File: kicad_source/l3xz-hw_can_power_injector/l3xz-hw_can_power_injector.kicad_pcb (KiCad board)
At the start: 2 copper layers, 43 x 23 mm, 17 parts, among them CN1 Conn_01x02, CN2 Conn_01x04, CN3 Conn_01x04, U1 RAA211650

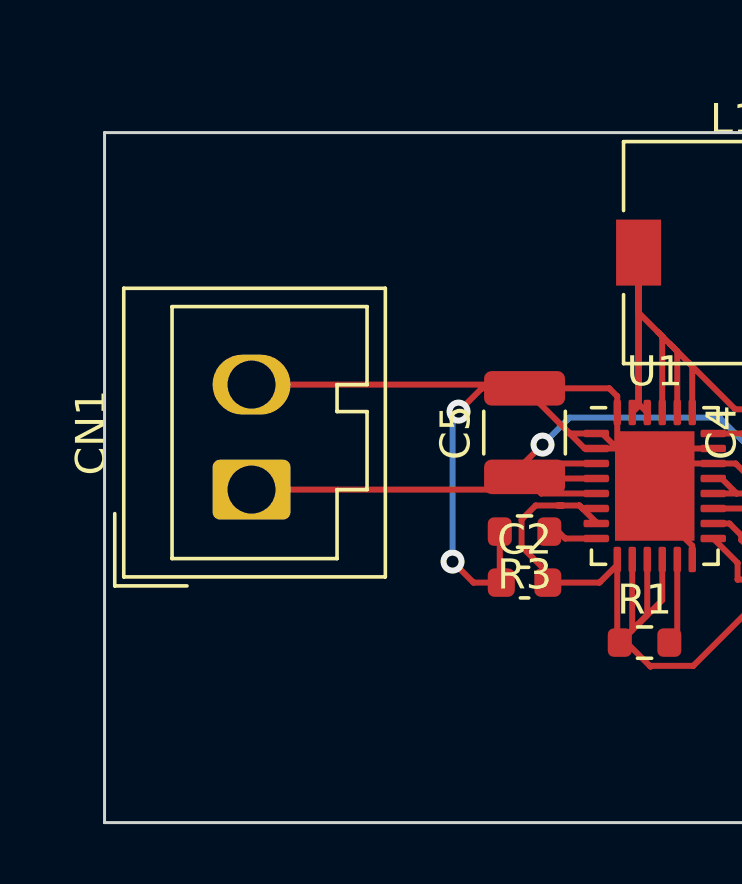
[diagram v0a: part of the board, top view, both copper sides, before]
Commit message: added Powerpole connector
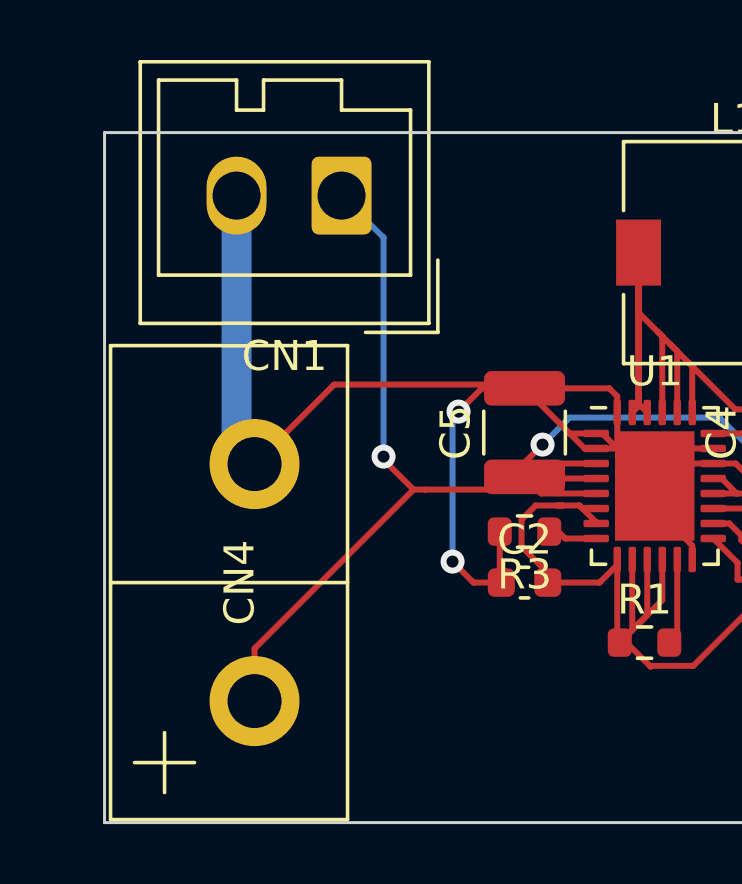
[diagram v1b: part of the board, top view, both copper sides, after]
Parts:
- added CN4: Conn_01x02, generationmake:POWERPOLE_2, F.Cu at (97.0, 102.0)
- moved CN1 10.2 mm to (99.9, 89.1), turned to 180 degrees
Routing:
- net +BATT: track 35.9 -> 50.6 mm, vias 2 -> 3
- net GND: track 101.6 -> 111.8 mm
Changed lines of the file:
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@@
   )
   (paper "A4")
+  (title_block
+    (title "l3xz-hw_can_power_injector")
+    (date "2022-10-25")
+    (rev "0.1")
+    (company "107-systems")
+  )
   (layers
     (0 "F.Cu" signal)
@@
     )
   )
+  (footprint "generationmake:POWERPOLE_2" (layer "F.Cu")
+    (at 97 102 90)
+    (property "Sheetfile" "Datei: l3xz-hw_can_power_injector.kicad_sch")
+    (property "Sheetname" "")
+    (attr through_hole)
+    (fp_text reference "CN4" (at 0 -0.5 90 unlocked) (layer "F.SilkS")
+      (effects (font (size 1 1) (thickness 0.15)))
+    )
+    (fp_text value "Conn_01x02" (at 0 1 90 unlocked) (layer "F.Fab")
+      (effects (font (size 1 1) (thickness 0.15)))
+    )
+    (fp_text user "${REFERENCE}" (at 0 2.5 90 unlocked) (layer "F.Fab")
+      (effects (font (size 1 1) (thickness 0.15)))
+    )
+    (fp_line (start 0 3.1) (end 0 -4.8) (layer "F.SilkS") (width 0.12))
+    (fp_line (start -7.9 3.1) (end 7.9 3.1) (layer "F.SilkS") (width 0.12))
+    (fp_line (start 7.9 3.1) (end 7.9 -4.8) (layer "F.SilkS") (width 0.12))
+    (fp_line (start 7.9 -4.8) (end -7.9 -4.8) (layer "F.SilkS") (width 0.12))
+    (fp_line (start -7.9 -4.8) (end -7.9 3.1) (layer "F.SilkS") (width 0.12))
+    (fp_line (start -7 -3) (end -5 -3) (layer "F.SilkS") (width 0.12))
+    (fp_line (start -6 -4) (end -6 -2) (layer "F.SilkS") (width 0.12))
+    (pad "1" thru_hole circle (at -3.95 0 90) (size 3 3) (drill 1.8) (layers *.Cu *.Mask)
+      (net 1 "+BATT") (pinfunction "Pin_1") (pintype "passive"))
+    (pad "2" thru_hole circle (at 3.95 0 90) (size 3 3) (drill 1.8) (layers *.Cu *.Mask)
+      (net 2 "GND") (pinfunction "Pin_2") (pintype "passive"))
+    (model "${KICAD6_3DMODEL_DIR}/generationmake/PP 15-45 (Std)-02-08-STEP.stp"
+      (offset (xyz 3.95 12.8 12))
+      (scale (xyz 1 1 1))
+      (rotate (xyz 90 0 0))
+    )
+    (model "${KICAD6_3DMODEL_DIR}/generationmake/PP 15-45 (Std)-02-08-STEP.stp"
+      (offset (xyz -3.95 12.8 12))
+      (scale (xyz 1 1 1))
+      (rotate (xyz 90 0 0))
+    )
+  )
   (footprint "Connector_Wago:Wago_734-132_1x02_P3.50mm_Vertical" (layer "F.Cu")
-    (at 96.9 98.9 90)
+    (at 99.9 89.1 180)
     (descr "Molex 734 Male header (for PCBs); Straight solder pin 1 x 1 mm, 734-132 , 2 Pins (http://www.farnell.com/datasheets/2157639.pdf), generated with kicad-footprint-generator")
     (tags "connector Wago  side entry")
@@
     (property "Sheetname" "")
     (attr through_hole)
-    (fp_text reference "CN1" (at 1.9 -5.35 90) (layer "F.SilkS")
-      (effects (font (size 1 1) (thickness 0.15)))
-    )
-    (fp_text value "Conn_01x02" (at 1.9 5.55 90) (layer "F.Fab")
-      (effects (font (size 1 1) (thickness 0.15)))
-    )
-    (fp_text user "${REFERENCE}" (at 1.9 3.65 90) (layer "F.Fab")
+    (fp_text reference "CN1" (at 1.9 -5.35) (layer "F.SilkS")
+      (effects (font (size 1 1) (thickness 0.15)))
+    )
+    (fp_text value "Conn_01x02" (at 1.9 5.55) (layer "F.Fab")
+      (effects (font (size 1 1) (thickness 0.15)))
+    )
+    (fp_text user "${REFERENCE}" (at 1.9 3.65) (layer "F.Fab")
       (effects (font (size 1 1) (thickness 0.15)))
     )
@@
     (fp_line (start -0.5 -4.15) (end 0 -3.442893) (layer "F.Fab") (width 0.1))
     (fp_line (start -2.8 -4.15) (end -2.8 4.35) (layer "F.Fab") (width 0.1))
-    (pad "1" thru_hole roundrect (at 0 0 90) (size 2 2.6) (drill 1.6) (layers *.Cu *.Mask) (roundrect_rratio 0.125)
+    (pad "1" thru_hole roundrect (at 0 0 180) (size 2 2.6) (drill 1.6) (layers *.Cu *.Mask) (roundrect_rratio 0.125)
       (net 1 "+BATT") (pinfunction "Pin_1") (pintype "passive"))
-    (pad "2" thru_hole oval (at 3.5 0 90) (size 2 2.6) (drill 1.6) (layers *.Cu *.Mask)
+    (pad "2" thru_hole oval (at 3.5 0 180) (size 2 2.6) (drill 1.6) (layers *.Cu *.Mask)
       (net 2 "GND") (pinfunction "Pin_2") (pintype "passive"))
     (model "${KICAD6_3DMODEL_DIR}/Connector_Wago.3dshapes/Wago_734-132_1x02_P3.50mm_Vertical.wrl"
@@
   (segment (start 113.07 99.03) (end 116.445 99.03) (width 0.2) (layer "F.Cu") (net 1))
   (segment (start 106 98) (end 106.6 97.4) (width 0.2) (layer "F.Cu") (net 1))
-  (segment (start 96.9 98.9) (end 105.575 98.9) (width 0.2) (layer "F.Cu") (net 1))
+  (segment (start 101.3 97.9) (end 101.3 97.8) (width 0.2) (layer "F.Cu") (net 1))
+  (segment (start 102.3 98.9) (end 101.3 97.9) (width 0.2) (layer "F.Cu") (net 1))
   (segment (start 108.39 99.03) (end 106.555 99.03) (width 0.2) (layer "F.Cu") (net 1))
+  (segment (start 102.7 98.9) (end 105.575 98.9) (width 0.2) (layer "F.Cu") (net 1))
   (segment (start 112.29 99.03) (end 113.07 99.03) (width 0.2) (layer "F.Cu") (net 1))
   (segment (start 106 98.475) (end 106 98) (width 0.2) (layer "F.Cu") (net 1))
@@
   (segment (start 115.425 98.475) (end 115.3 98.6) (width 0.2) (layer "F.Cu") (net 1))
   (segment (start 106.555 99.03) (end 106 98.475) (width 0.2) (layer "F.Cu") (net 1))
+  (segment (start 102.7 98.9) (end 102.3 98.9) (width 0.2) (layer "F.Cu") (net 1))
+  (segment (start 97 104.2) (end 97 105.95) (width 0.2) (layer "F.Cu") (net 1))
   (segment (start 112.29 98.53) (end 112.57 98.53) (width 0.2) (layer "F.Cu") (net 1))
   (segment (start 106.445 98.03) (end 106 98.475) (width 0.2) (layer "F.Cu") (net 1))
   (segment (start 108.39 98.03) (end 106.445 98.03) (width 0.2) (layer "F.Cu") (net 1))
+  (segment (start 102.3 98.9) (end 97 104.2) (width 0.2) (layer "F.Cu") (net 1))
   (segment (start 108.39 98.53) (end 106.055 98.53) (width 0.2) (layer "F.Cu") (net 1))
   (segment (start 115.3 98.6) (end 115.340853 98.640853) (width 0.2) (layer "F.Cu") (net 1))
@@
   (segment (start 106.055 98.53) (end 106 98.475) (width 0.2) (layer "F.Cu") (net 1))
   (via (at 106.6 97.4) (size 0.8) (drill 0.4) (layers "F.Cu" "B.Cu") (net 1))
+  (via (at 101.3 97.8) (size 0.8) (drill 0.4) (layers "F.Cu" "B.Cu") (net 1))
   (via (at 115.340853 98.640853) (size 0.8) (drill 0.4) (layers "F.Cu" "B.Cu") (net 1))
+  (segment (start 101.3 90.5) (end 99.9 89.1) (width 0.2) (layer "B.Cu") (net 1))
   (segment (start 114.640853 98.640853) (end 112.5 96.5) (width 0.2) (layer "B.Cu") (net 1))
   (segment (start 115.340853 98.640853) (end 114.640853 98.640853) (width 0.2) (layer "B.Cu") (net 1))
   (segment (start 107.5 96.5) (end 106.6 97.4) (width 0.2) (layer "B.Cu") (net 1))
+  (segment (start 101.3 97.8) (end 101.3 90.5) (width 0.2) (layer "B.Cu") (net 1))
   (segment (start 112.5 96.5) (end 107.5 96.5) (width 0.2) (layer "B.Cu") (net 1))
   (segment (start 125.625 94.875) (end 122.6 94.875) (width 0.2) (layer "F.Cu") (net 2))
@@
   (segment (start 124.9 96.8) (end 124.9 95.6) (width 0.2) (layer "F.Cu") (net 2))
   (segment (start 127.075 104.875) (end 124.9 102.7) (width 0.2) (layer "F.Cu") (net 2))
-  (segment (start 96.9 95.4) (end 105.875 95.4) (width 0.2) (layer "F.Cu") (net 2))
   (segment (start 106 95.525) (end 104.575 95.525) (width 0.2) (layer "F.Cu") (net 2))
   (segment (start 123.9 96.4) (end 124.5 96.4) (width 0.2) (layer "F.Cu") (net 2))
   (segment (start 107.4375 96.9625) (end 106 95.525) (width 0.2) (layer "F.Cu") (net 2))
+  (segment (start 99.65 95.4) (end 105.875 95.4) (width 0.2) (layer "F.Cu") (net 2))
   (segment (start 108.39 97.03) (end 108.59 97.03) (width 0.2) (layer "F.Cu") (net 2))
   (segment (start 129.05 104.875) (end 127.075 104.875) (width 0.2) (layer "F.Cu") (net 2))
+  (segment (start 105.875 95.4) (end 106 95.525) (width 0.2) (layer "F.Cu") (net 2))
   (segment (start 122.6 94.875) (end 121 96.475) (width 0.2) (layer "F.Cu") (net 2))
   (segment (start 129.05 94.875) (end 125.625 94.875) (width 0.2) (layer "F.Cu") (net 2))
@@
   (segment (start 104.3 102) (end 103.6 101.3) (width 0.2) (layer "F.Cu") (net 2))
   (segment (start 115.5 101.775) (end 118 101.775) (width 0.2) (layer "F.Cu") (net 2))
-  (segment (start 105.875 95.4) (end 106 95.525) (width 0.2) (layer "F.Cu") (net 2))
   (segment (start 112.29 97.53) (end 111.59 97.53) (width 0.2) (layer "F.Cu") (net 2))
   (segment (start 109.09 95.79) (end 108.825 95.525) (width 0.2) (layer "F.Cu") (net 2))
@@
   (segment (start 110.34 99.517652) (end 111.59 100.767652) (width 0.2) (layer "F.Cu") (net 2))
   (segment (start 118 88.225) (end 120.7 88.225) (width 0.2) (layer "F.Cu") (net 2))
+  (segment (start 97 98.05) (end 99.65 95.4) (width 0.2) (layer "F.Cu") (net 2))
   (via (at 103.6 101.3) (size 0.8) (drill 0.4) (layers "F.Cu" "B.Cu") (net 2))
   (via (at 124.8 88.6) (size 0.8) (drill 0.4) (layers "F.Cu" "B.Cu") (net 2))
@@
   (segment (start 103.6 101.3) (end 103.6 96.5) (width 0.2) (layer "B.Cu") (net 2))
   (segment (start 103.6 96.5) (end 103.8 96.3) (width 0.2) (layer "B.Cu") (net 2))
+  (segment (start 96.4 97.45) (end 97 98.05) (width 1) (layer "B.Cu") (net 2))
+  (segment (start 96.4 89.1) (end 96.4 97.45) (width 1) (layer "B.Cu") (net 2))
   (segment (start 124.8 95.5) (end 123.9 96.4) (width 0.2) (layer "B.Cu") (net 2))
   (segment (start 124.8 88.6) (end 124.8 95.5) (width 0.2) (layer "B.Cu") (net 2))

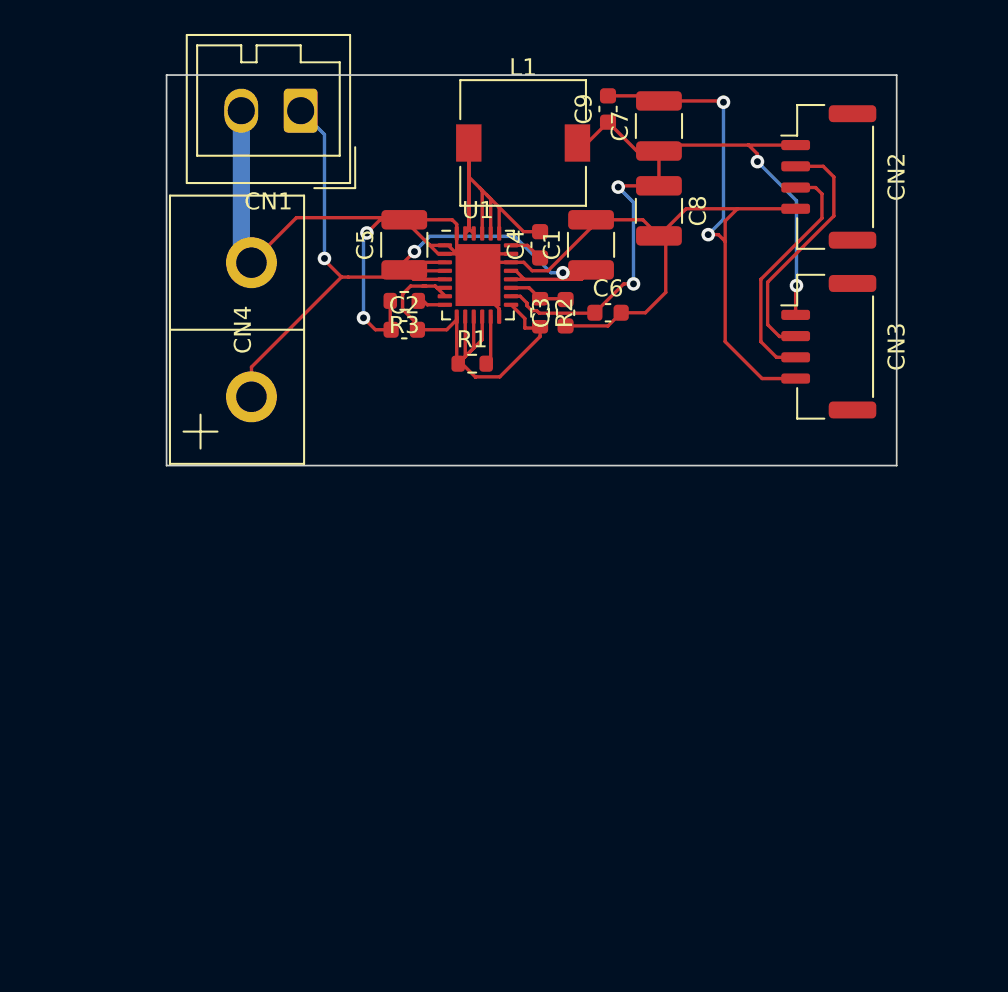
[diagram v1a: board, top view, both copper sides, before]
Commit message: addedhoricontal powerpole
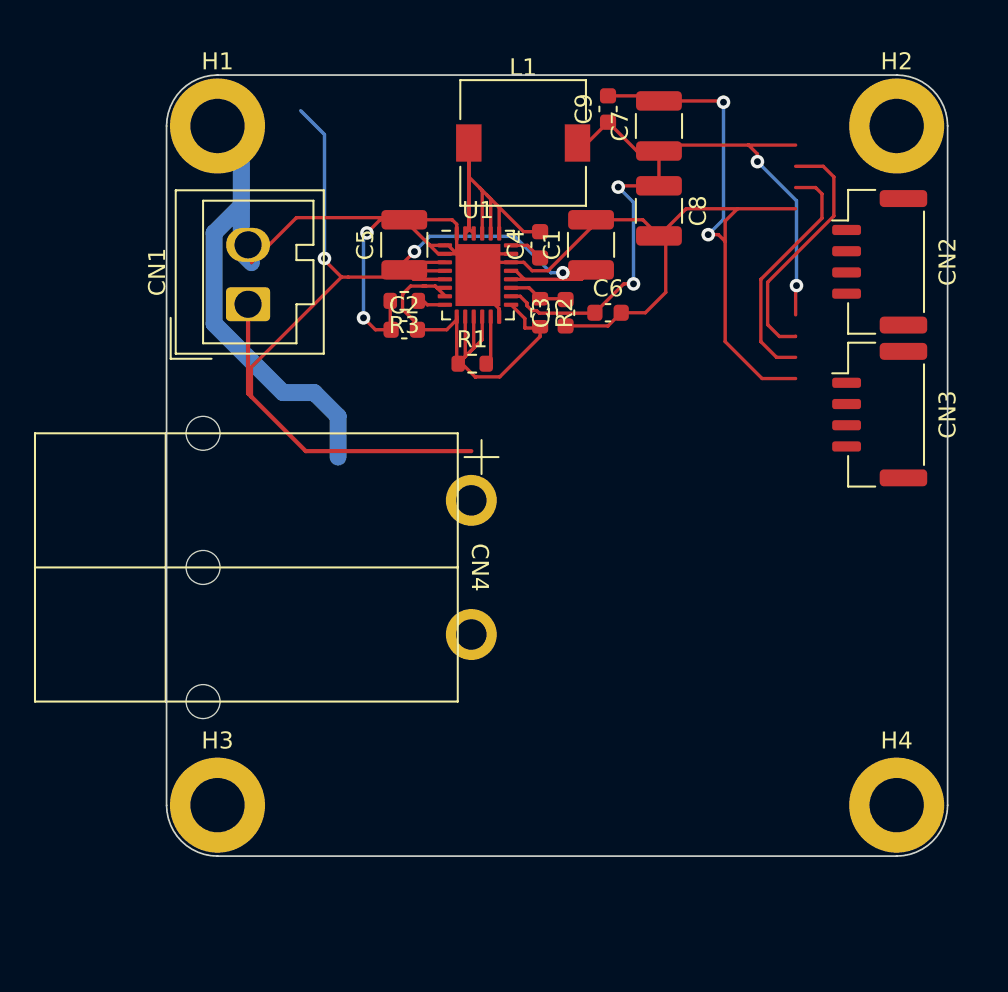
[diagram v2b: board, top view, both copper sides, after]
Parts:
- added H1: MountingHole_Pad, MountingHole:MountingHole_3.2mm_M3_DIN965_Pad, F.Cu at (95.0, 90.0)
- added H2: MountingHole_Pad, MountingHole:MountingHole_3.2mm_M3_DIN965_Pad, F.Cu at (135.0, 90.0)
- added H3: MountingHole_Pad, MountingHole:MountingHole_3.2mm_M3_DIN965_Pad, F.Cu at (95.0, 130.0)
- added H4: MountingHole_Pad, MountingHole:MountingHole_3.2mm_M3_DIN965_Pad, F.Cu at (135.0, 130.0)
- CN4: footprint generationmake:POWERPOLE_2 -> generationmake:POWERPOLE_hor_2
- moved CN4 19.1 mm to (110.0, 116.0), turned to -90 degrees
- moved CN1 11.8 mm to (96.8, 100.5), turned to 90 degrees
- moved CN2 5.83 mm to (134.0, 98.0)
- moved CN3 5.00 mm to (134.0, 107.0)
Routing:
- net +BATT: track 50.6 -> 70.4 mm
- net GND: track 111.8 -> 131.3 mm
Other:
- board size 43 x 23 mm -> 46 x 46 mm

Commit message: added second uavcan channel and diodes
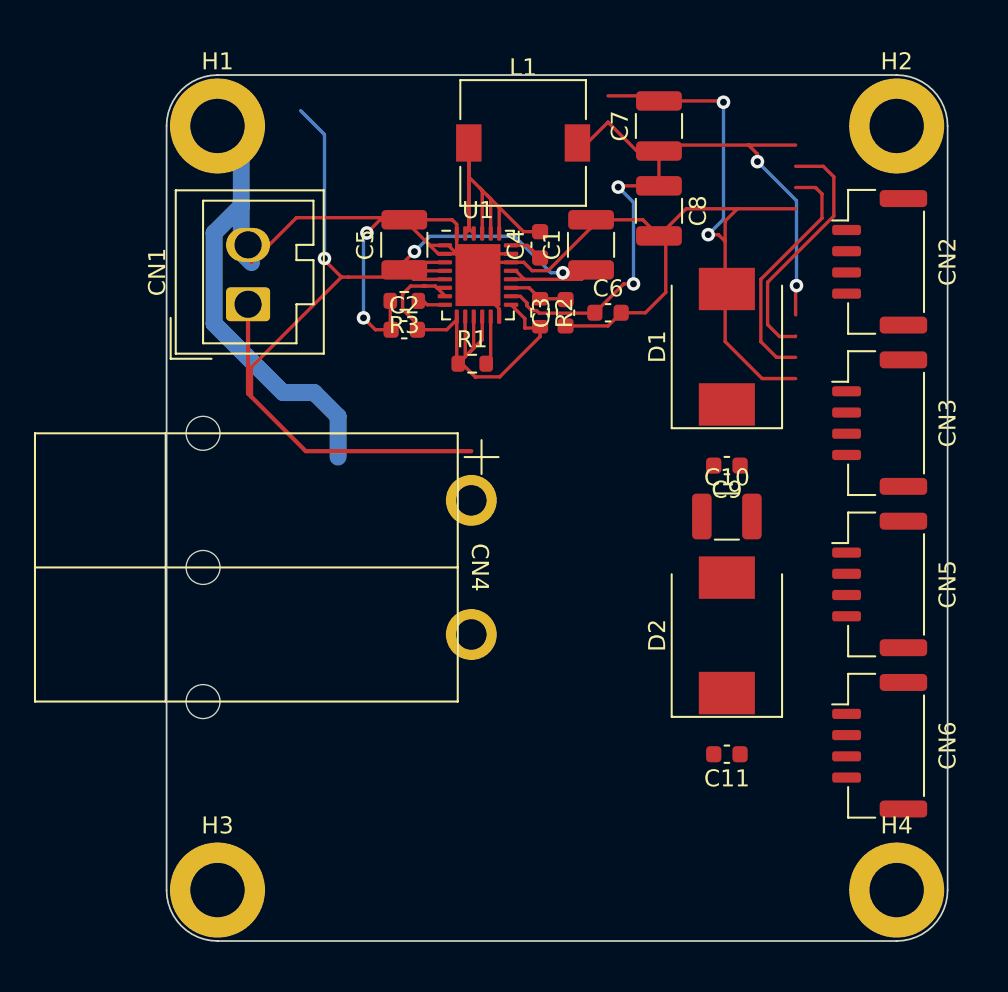
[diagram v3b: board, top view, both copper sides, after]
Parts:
- added C10: C_Small, Capacitor_SMD:C_1210_3225Metric, F.Cu at (125.0, 113.0)
- added C11: C_Small, Capacitor_SMD:C_0603_1608Metric, F.Cu at (125.0, 127.0)
- added CN5: Conn_01x04, Connector_JST:JST_GH_BM04B-GHS-TBT_1x04-1MP_P1.25mm_Vertical, F.Cu at (134.0, 117.0)
- added CN6: Conn_01x04, Connector_JST:JST_GH_BM04B-GHS-TBT_1x04-1MP_P1.25mm_Vertical, F.Cu at (134.0, 126.5)
- added D1: B520C, Diode_SMD:D_SMC, F.Cu at (125.0, 103.0)
- added D2: B520C, Diode_SMD:D_SMC, F.Cu at (125.0, 120.0)
- moved C9 22.1 mm to (125.0, 110.0), turned to 180 degrees
- moved H3 5.00 mm to (95.0, 135.0)
- moved H4 5.00 mm to (135.0, 135.0)
- moved CN3 0.50 mm to (134.0, 107.5)
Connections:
- net /CANH renamed /CAN1H
- net /CANL renamed /CAN1L
- C9 pad 1: VCC -> /CAN1VCC
- CN2 pad 1: VCC -> /CAN1VCC
- CN3 pad 1: VCC -> /CAN1VCC
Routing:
- net (no net): track 0.00 -> 29.1 mm
- net /CAN1H: track 14.8 -> 0.00 mm
- net /CAN1L: track 14.3 -> 0.00 mm
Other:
- board size 46 x 46 mm -> 46 x 51 mm
